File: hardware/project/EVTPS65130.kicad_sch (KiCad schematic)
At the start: 32 parts, among them J1 USB_C_Receptacle_USB2.0_14P, Q10 PMOS, U3 TPS65130RGE

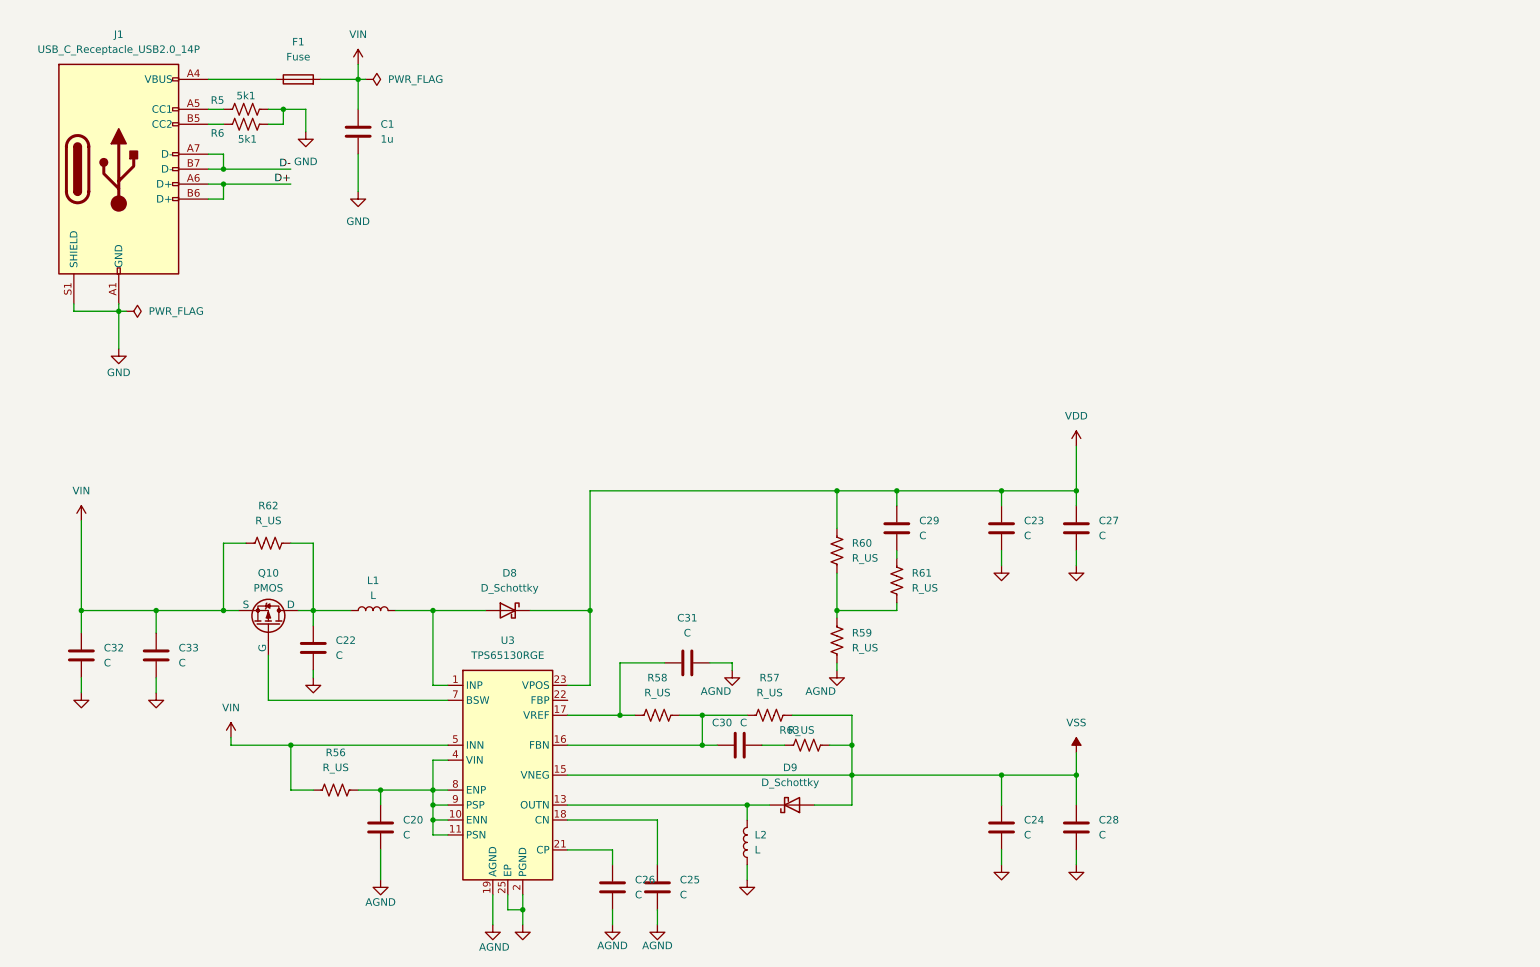
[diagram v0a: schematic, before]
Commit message: Added: output filter, values
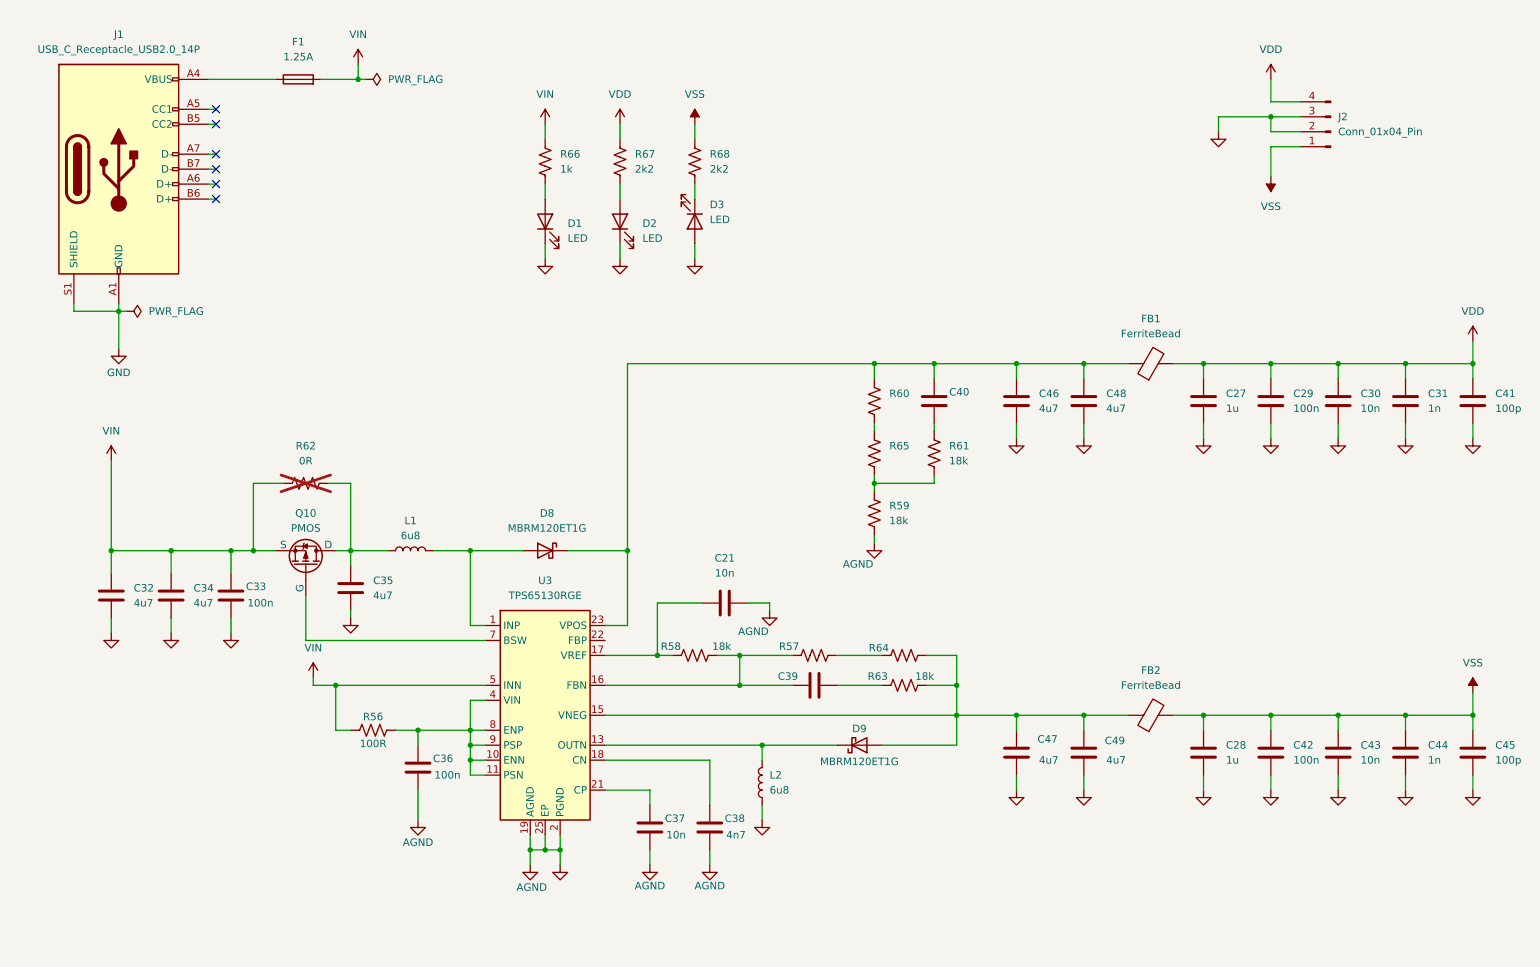
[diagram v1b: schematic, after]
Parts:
- removed C1: 1u, Capacitor_SMD:C_0603_1608Metric_Pad1.08x0.95mm_HandSolder, symbol Device:C
- removed C20, C22, C23, C24, C25, C26: C, symbol Device:C
- removed R5, R6: 5k1, Resistor_SMD:R_0402_1005Metric_Pad0.72x0.64mm_HandSolder, symbol Device:R_US
- added C21, C37, C43: 10n, symbol Device:C
- added C34, C35, C46, C47, C48, C49: 4u7, symbol Device:C
- added C36, C42: 100n, symbol Device:C
- added C38: 4n7, symbol Device:C
- added C39, C40: (no value), symbol Device:C
- added C41, C45: 100p, symbol Device:C
- added C44: 1n, symbol Device:C
- added D1, D2, D3: LED, symbol Device:LED
- added FB1, FB2: FerriteBead, symbol Device:FerriteBead
- added J2: Conn_01x04_Pin, symbol Connector:Conn_01x04_Pin
- added R64, R65: (no value), symbol Device:R_US
- added R66: 1k, symbol Device:R_US
- added R67, R68: 2k2, symbol Device:R_US
- C27, C28: value C -> 1u
- C29, C33: value C -> 100n
- C30: value C -> 10n
- C31: value C -> 1n
- C32: value C -> 4u7
- D8, D9: value D_Schottky -> MBRM120ET1G
- F1: value Fuse -> 1.25A
- L1, L2: value L -> 6u8
- R56: value R_US -> 100R
- R57, R60: value R_US -> (none)
- R58, R59, R61, R63: value R_US -> 18k
- R62: value R_US -> 0R; now not fitted
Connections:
- net GND is gone; now on net AGND: C27.2, C28.2, C32.2, C33.2, J1.A1 (GND), J1.A12 (GND), J1.B1 (GND), J1.B12 (GND), J1.S1 (SHIELD), L2.1, U3.2 (PGND), U3.25 (EP), U3.3 (PGND)
- net AGND: now also C29.2, C30.2, C21.2, C34.2, C35.2, C36.2, C37.2, C38.2, C41.2, C42.2, C43.2, C44.2, C45.2, C46.2, C47.2, C48.2, C49.2, D1.1 (K), D2.1 (K), D3.2 (A), J2.2 (Pin_2), J2.3 (Pin_3)
- net VDD: now also C30.1, C31.1, C41.1, FB1.2, J2.4 (Pin_4), R67.2; no longer D8.1 (K), R60.2, U3.23 (VPOS)
- net VIN: now also C34.1, R66.2
- net VSS: now also C42.1, C43.1, C44.1, C45.1, FB2.2, J2.1 (Pin_1), R68.2; no longer D9.2 (A), R57.2, R63.2, U3.15 (VNEG)
- net at R56.2, U3.10 (ENN), U3.11 (PSN)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: now also C36.1
- net at R57.1, R58.2, U3.16 (FBN): now also C39.1; no longer C30.1
- net at L1.1, Q10.1 (D), R62.2: now also C35.1
- net at R61.1: now also C40.2; no longer C29.2
- net at R59.1, R61.2: now also R65.1; no longer R60.1
- net at R63.1: now also C39.2; no longer C30.2
- net at U3.21 (CP): now also C37.1
- net at R58.1, U3.17 (VREF): now also C21.1; no longer C31.1
- net at U3.18 (CN): now also C38.1
- net D+: no longer names the net of J1.A6 (D+)
- net D+: no longer J1.B6 (D+)
- net D-: no longer names the net of J1.A7 (D-)
- net D-: no longer J1.B7 (D-)
- new net: D3.1 (K), R68.1
- new net: R60.1, R65.2
- new net: D2.2 (A), R67.1
- new net: R57.2, R64.1
- new net: C47.1, C49.1, D9.2 (A), FB2.1, R63.2, R64.2, U3.15 (VNEG)
- new net: C40.1, C46.1, C48.1, D8.1 (K), FB1.1, R60.2, U3.23 (VPOS)
- new net: D1.2 (A), R66.1
- no-connect marks 0 -> 6
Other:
- moved on the sheet: C27, C32, C33, D8, L1, Q10, R56, R57, R58, R59, R60, R61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

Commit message: Update: added footprint
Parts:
- removed J1: USB_C_Receptacle_USB2.0_14P, Connector_USB:USB_C_Receptacle_GCT_USB4105-xx-A_16P_TopMnt_Horizontal, symbol Connector:USB_C_Receptacle_USB2.0_14P
- added J1: USB_C_Receptacle_PowerOnly_6P, symbol Connector:USB_C_Receptacle_PowerOnly_6P
- added R69, R70: 5k1, Resistor_SMD:R_0402_1005Metric, symbol Device:R_US
- C21, C29, C30, C31, C33, C36, C37, C38, C39, C40, C41, C42, C43, C44, C45: footprint (none) -> Capacitor_SMD:C_0402_1005Metric
- C27, C28: footprint (none) -> Capacitor_SMD:C_0603_1608Metric
- C32, C34, C35, C46, C47, C48, C49: footprint (none) -> Capacitor_SMD:C_1206_3216Metric
- D1, D2, D3: footprint (none) -> LED_SMD:LED_0603_1608Metric
- D8, D9: footprint (none) -> Diode_SMD:D_SMA
- FB1, FB2: footprint (none) -> Inductor_SMD:L_0805_2012Metric
- J2: footprint (none) -> Connector_PinHeader_2.54mm:PinHeader_1x04_P2.54mm_Vertical
- L1, L2: footprint (none) -> EVTPS65130_lib:74406032068; MPN (none) -> 74406032068; Manufacturer (none) -> Wurth
- Q10: footprint (none) -> Package_TO_SOT_SMD:SOT-23
- R56, R57, R58, R59, R60, R61, R63, R64, R65, R66, R67, R68: footprint (none) -> Resistor_SMD:R_0402_1005Metric
- R62: footprint (none) -> Resistor_SMD:R_0805_2012Metric
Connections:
- net AGND: now also J1.A12 (GND), J1.B12 (GND), J1.SH (SHIELD), R69.2, R70.1
- net at R59.1, R61.2, R65.1: now also U3.22 (FBP)
- net at F1.1: now also J1.A9 (VBUS), J1.B9 (VBUS)
- new net: J1.B5 (CC2), R70.2
- new net: J1.A5 (CC1), R69.1
- no-connect marks 6 -> 0
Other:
- moved on the sheet: D3, R68

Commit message: Started PCB placement
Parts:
- J1: footprint (none) -> Connector_USB:USB_C_Receptacle_GCT_USB4125-xx-x-0190_6P_TopMnt_Horizontal
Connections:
- net AGND: no longer C27.2, C28.2, C29.2, C30.2, C31.2, C32.2, C33.2, C34.2, C35.2, C41.2, C42.2, C43.2, C44.2, C45.2, C46.2, C47.2, C48.2, C49.2, D1.1 (K), D2.1 (K), D3.2 (A), J1.A12 (GND), J1.B12 (GND), J1.SH (SHIELD), J2.2 (Pin_2), J2.3 (Pin_3), L2.1, R69.2, R70.1, U3.2 (PGND), U3.25 (EP), U3.3 (PGND)
- new net GND: C27.2, C28.2, C29.2, C30.2, C31.2, C32.2, C33.2, C34.2, C35.2, C41.2, C42.2, C43.2, C44.2, C45.2, C46.2, C47.2, C48.2, C49.2, D1.1 (K), D2.1 (K), D3.2 (A), J1.A12 (GND), J1.B12 (GND), J1.SH (SHIELD), J2.2 (Pin_2), J2.3 (Pin_3), L2.1, R69.2, R70.1, U3.2 (PGND), U3.25 (EP), U3.3 (PGND)
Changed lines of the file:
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@@
 	)
 	(junction
-		(at 97.79 156.21)
-		(diameter 0)
-		(color 0 0 0 0)
-	)
-	(junction
 		(at 166.37 73.66)
 		(diameter 0)
@@
 		(color 0 0 0 0)
 	)
-	(junction
-		(at 100.33 156.21)
-		(diameter 0)
-		(color 0 0 0 0)
-	)
 	(wire
 		(pts
@@
 	(wire
 		(pts
-			(xy 97.79 153.67) (xy 97.79 156.21)
-		)
-		(stroke
-			(width 0)
-			(type default)
-		)
-	)
-	(wire
-		(pts
 			(xy 246.38 133.35) (xy 234.95 133.35)
 		)
@@
 	(wire
 		(pts
-			(xy 97.79 156.21) (xy 97.79 158.75)
+			(xy 97.79 153.67) (xy 97.79 158.75)
 		)
 		(stroke
@@
 	(wire
 		(pts
-			(xy 97.79 156.21) (xy 100.33 156.21)
-		)
-		(stroke
-			(width 0)
-			(type default)
-		)
-	)
-	(wire
-		(pts
 			(xy 55.88 40.64) (xy 53.34 40.64)
 		)
@@
 			)
 		)
-		(property "Footprint" ""
+		(property "Footprint" "Connector_USB:USB_C_Receptacle_GCT_USB4125-xx-x-0190_6P_TopMnt_Horizontal"
 			(at 31.75 30.48 0)
 			(hide yes)
